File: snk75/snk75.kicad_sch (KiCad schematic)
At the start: 17 parts

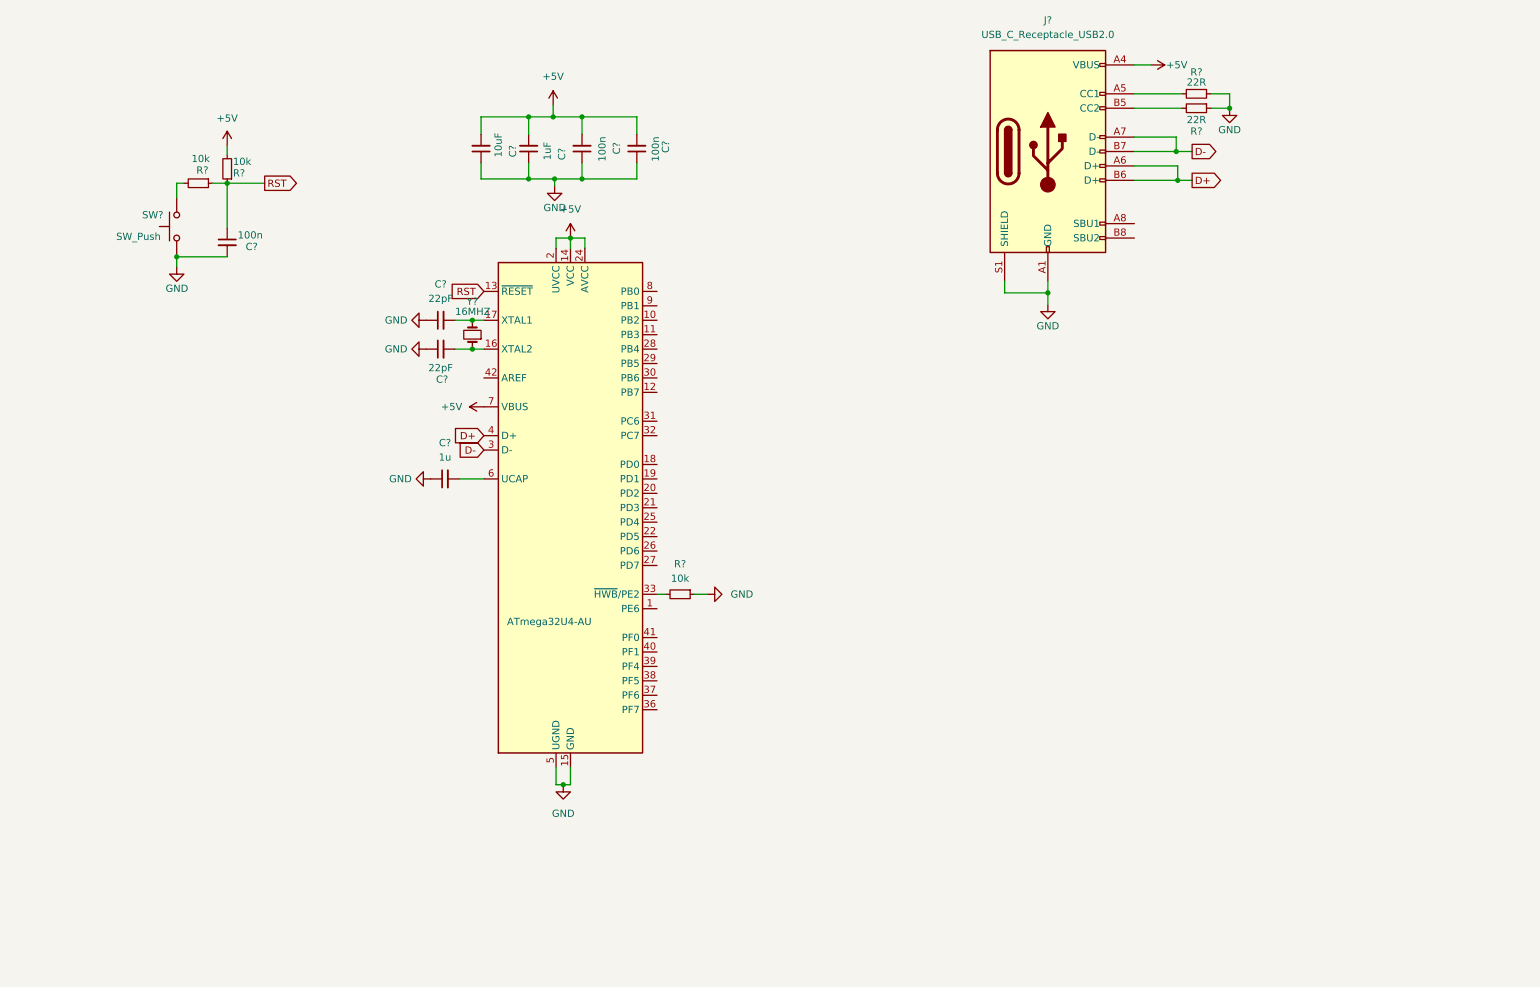
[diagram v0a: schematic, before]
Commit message: Add ubc c connector
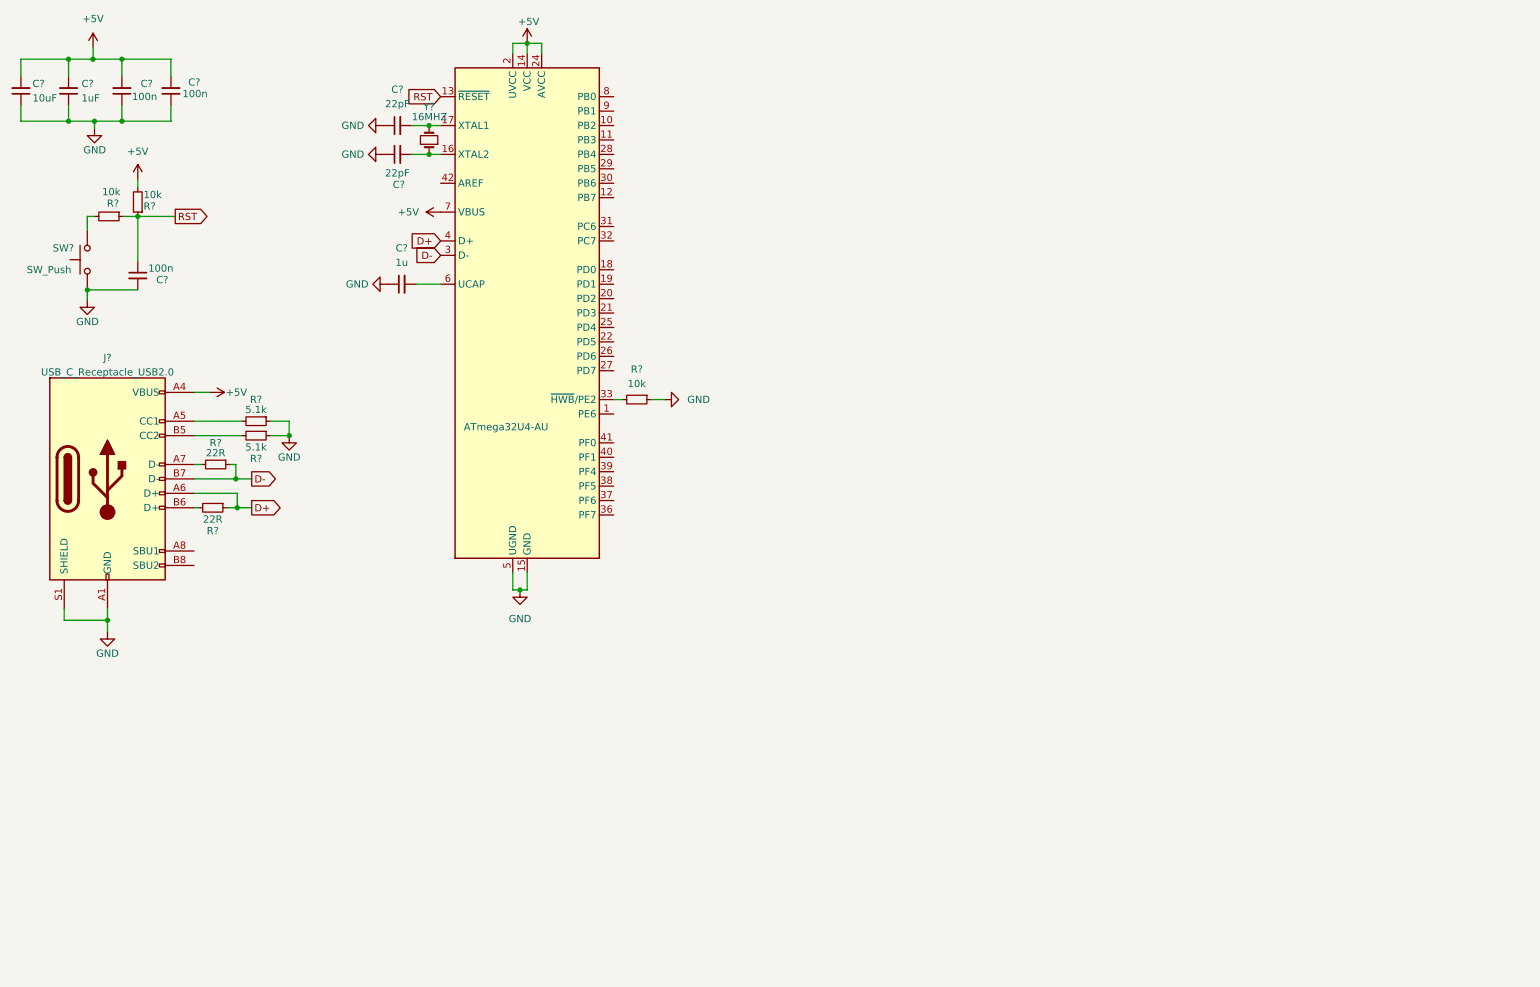
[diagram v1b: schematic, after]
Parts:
- added R? (x2): 22R, symbol Device:R_Small
- R? (x2): value 22R -> 5.1k
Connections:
- net D+: now also R?.1; no longer J?.B6 (D+)
- net D-: now also R?.1; no longer J?.A7 (D-)
- new net: J?.A7 (D-), R?.2
- new net: J?.B6 (D+), R?.2
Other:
- moved on the sheet: 1uF, C?, J?, R?, SW?, Y?

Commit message: Start keys layout
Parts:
- removed R?: 10k, symbol Device:R_Small
- added R1: 330, Resistor_SMD:R_1206_3216Metric_Pad1.30x1.75mm_HandSolder, symbol Device:R_Small
- 1uF1: renamed from 1uF; footprint (none) -> Capacitor_SMD:C_0805_2012Metric_Pad1.18x1.45mm_HandSolder
- C1, C2, C3, C4, C5, C6, C7: renamed from C?; footprint (none) -> Capacitor_SMD:C_0805_2012Metric_Pad1.18x1.45mm_HandSolder
- J1: renamed from J?; footprint (none) -> Connector_USB:USB_C_Receptacle_Palconn_UTC16-G
- R2, R3, R4, R5, R6: renamed from R?; footprint (none) -> Resistor_SMD:R_1206_3216Metric_Pad1.30x1.75mm_HandSolder
- R7: renamed from R?; value 10k -> 1k; footprint (none) -> Resistor_SMD:R_1206_3216Metric_Pad1.30x1.75mm_HandSolder
- SWP1: renamed from SW?; footprint (none) -> Button_Switch_SMD:SW_MEC_5GSH9
- Y1: renamed from Y?; footprint (none) -> Crystal:Crystal_SMD_5032-2Pin_5.0x3.2mm_HandSoldering
- renumbered U to U1
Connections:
- net GND: now also R1.2; no longer C3.2
- net RST: now also SWP1.2
- new net: C3.2, R1.1
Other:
- added sheet Keys (keys.kicad_sch)
- moved on the sheet: 1uF1, C1, C2, C3, C4, C5, C6, C7, J1, R2, R3, R4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

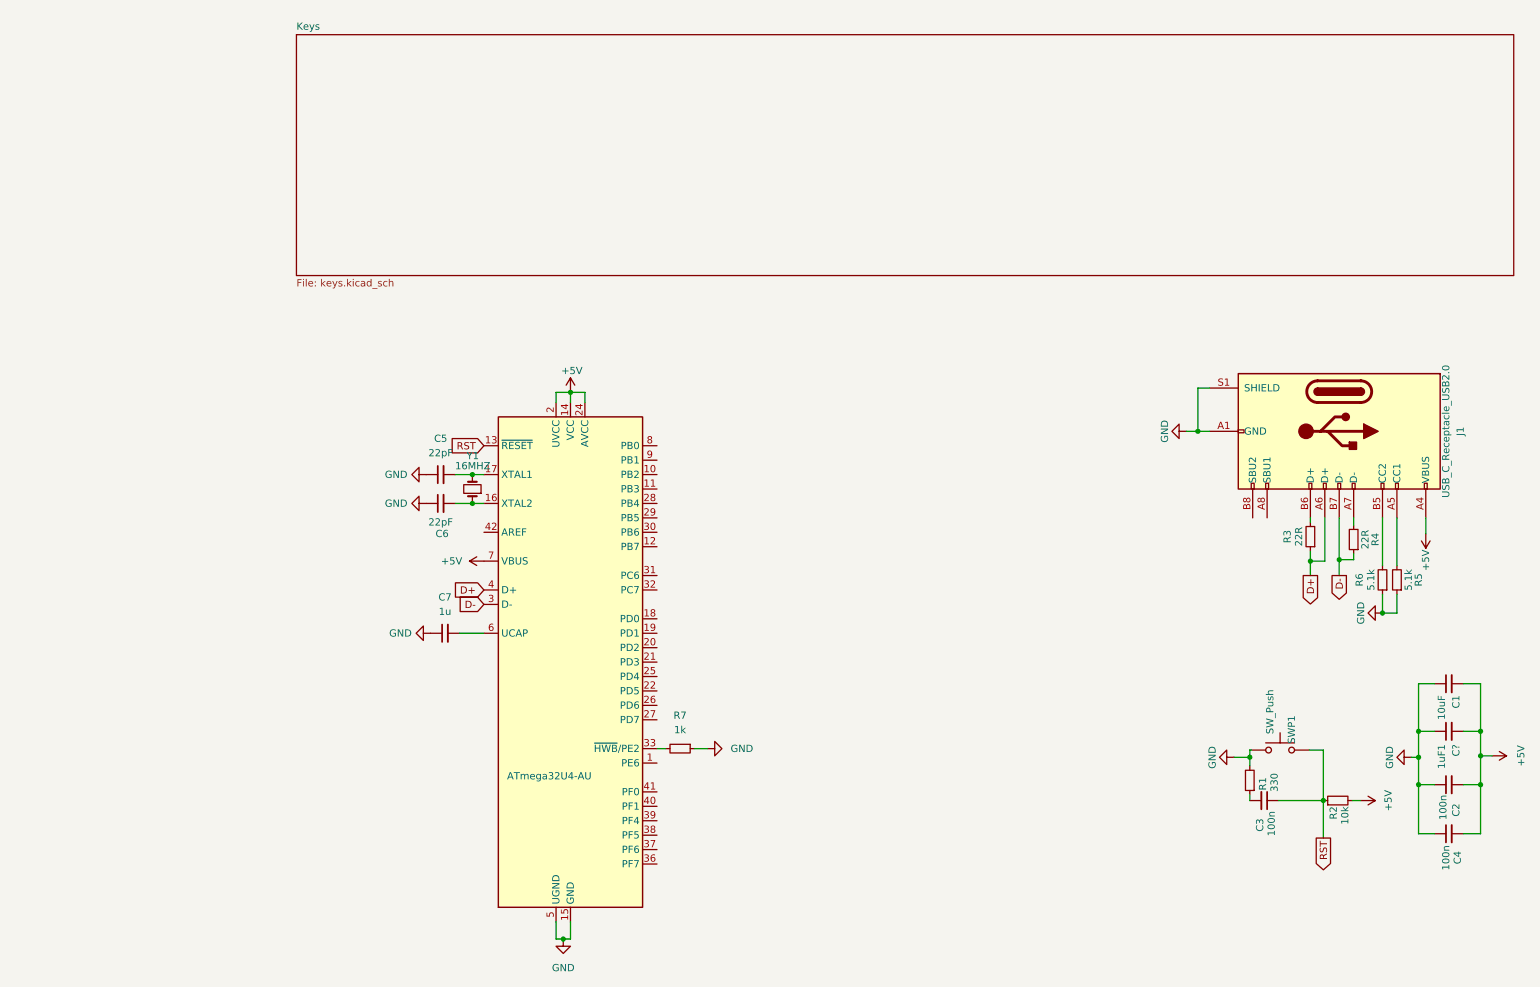
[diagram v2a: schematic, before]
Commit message: feat: keyboard keys
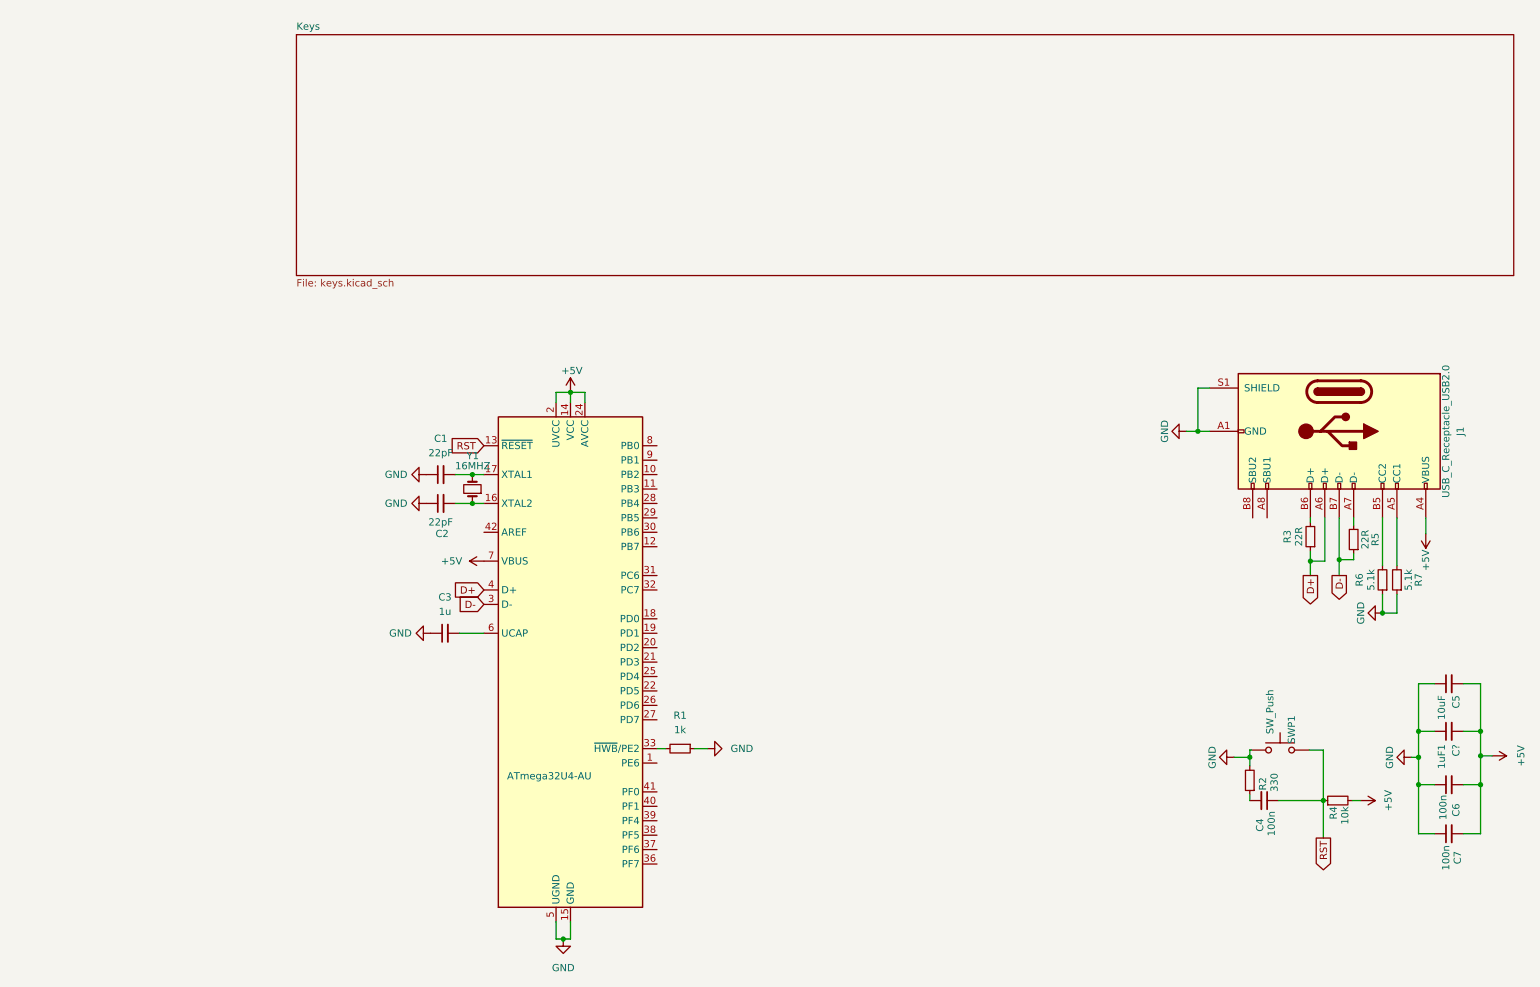
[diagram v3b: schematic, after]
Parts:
- renumbered C5 to C1, C6 to C2, C7 to C3, C3 to C4, C1 to C5, C2 to C6, C4 to C7, R7 to R1, R1 to R2, R2 to R4, R4 to R5, R5 to R7
